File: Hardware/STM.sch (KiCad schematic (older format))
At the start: 17 parts, among them U1 STM32F042K6Ux

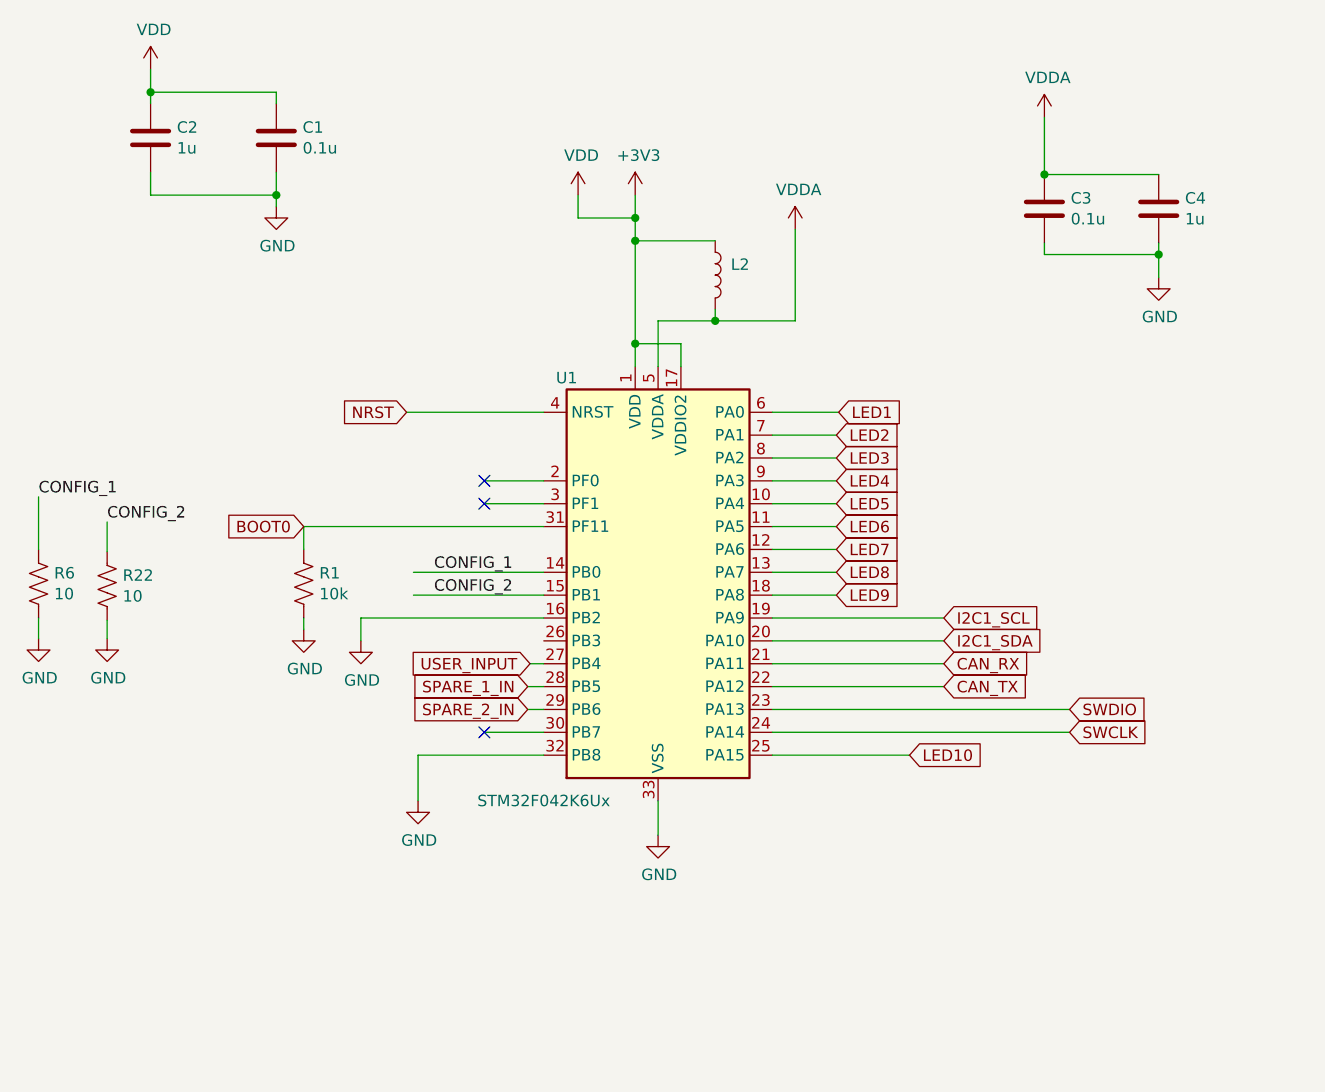
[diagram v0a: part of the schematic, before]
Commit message: Rev B
Update STM package, switcher circuit, layout
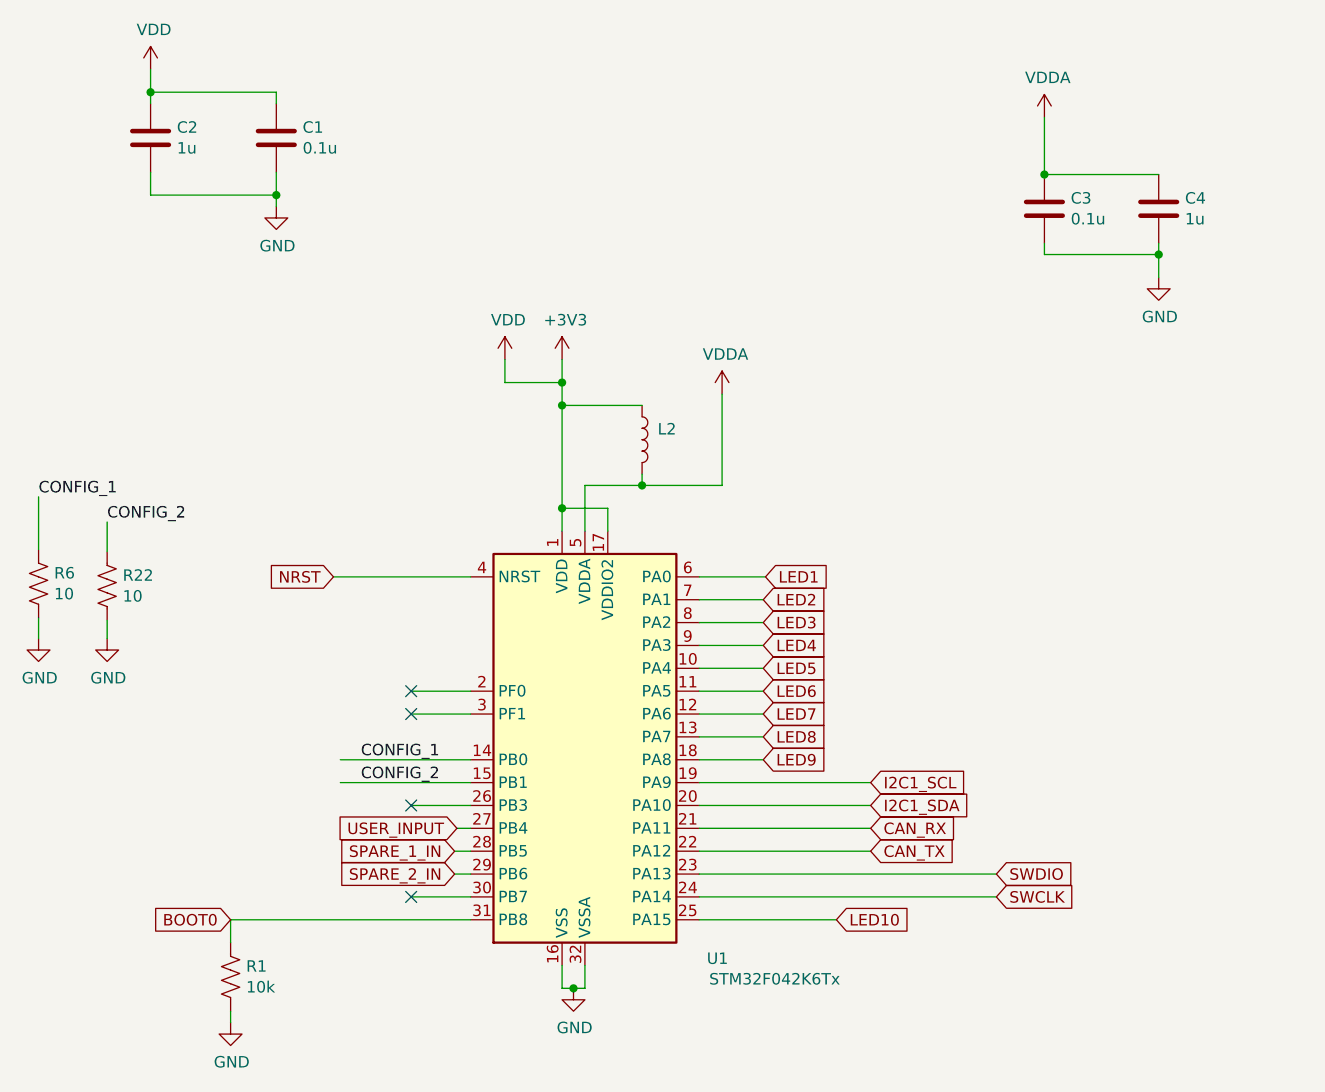
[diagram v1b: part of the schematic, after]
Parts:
- removed U1: STM32F042K6Ux, Package_DFN_QFN:QFN-32-1EP_5x5mm_P0.5mm_EP3.45x3.45mm, symbol MCU_ST_STM32F0:STM32F042K6Ux
- added U1: STM32F042K6Tx, Package_QFP:LQFP-32_7x7mm_P0.8mm, symbol MCU_ST_STM32F0:STM32F042K6Tx
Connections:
- net +3V3: now also U1.1 (VDD), U1.17 (VDDIO2)
- net BOOT0: now also U1.31 (PB8)
- net CAN_RX: now also U1.21 (PA11)
- net CAN_TX: now also U1.22 (PA12)
- net CONFIG_1: now also U1.14 (PB0)
- net CONFIG_2: now also U1.15 (PB1)
- net GND: now also U1.16 (VSS), U1.32 (VSSA)
- net I2C1_SCL: now also U1.19 (PA9)
- net I2C1_SDA: now also U1.20 (PA10)
- net LED1: now also U1.6 (PA0)
- net LED10: now also U1.25 (PA15)
- net LED2: now also U1.7 (PA1)
- net LED3: now also U1.8 (PA2)
- net LED4: now also U1.9 (PA3)
- net LED5: now also U1.10 (PA4)
- net LED6: now also U1.11 (PA5)
- net LED7: now also U1.12 (PA6)
- net LED8: now also U1.13 (PA7)
- net LED9: now also U1.18 (PA8)
- net NRST: now also U1.4 (NRST)
- net SPARE_1_IN: now also U1.28 (PB5)
- net SPARE_2_IN: now also U1.29 (PB6)
- net SWCLK: now also U1.24 (PA14)
- net SWDIO: now also U1.23 (PA13)
- net USER_INPUT: now also U1.27 (PB4)
- net VDDA: now also U1.5 (VDDA)
- no-connect marks 3 -> 4
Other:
- moved on the sheet: L2, R1

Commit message: Update components for assembly, generate gerbers
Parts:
- C1, C3: Comments (none) -> 0402 Multilayer Ceramic Capacitors MLCC - SMD/SMT ROHS; LCSC (none) -> C2655418
- C2: Comment (none) -> X5R ±10% 10V 1uF 0402 Multilayer Ceramic Capacitors MLCC - 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; LCSC (none) -> C389008
- C4: Comments (none) -> X5R ±10% 10V 1uF 0402 Multilayer Ceramic Capacitors MLCC - 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; LCSC (none) -> C389008
- L2: Comments (none) -> 600Ω @ 100MHz 1 500mA 340mΩ 0402 Ferrite Beads ROHS; LCSC (none) -> C76886; Part Number BLM15PE300SH1D -> (none)
- R22, R6: value 10 -> 10k
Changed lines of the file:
@@
 F 2 "Capacitor_SMD:C_0402_1005Metric" H 5978 3020 50  0001 C CNN
 F 3 "~" H 5940 3170 50  0001 C CNN
+F 4 "C389008" H 5940 3170 50  0001 C CNN "LCSC"
+F 5 "X5R ±10% 10V 1uF 0402 Multilayer Ceramic Capacitors MLCC - SMD/SMT ROHS" H 5940 3170 50  0001 C CNN "Comments"
 	1    5940 3170
 	1    0    0    -1
@@
 F 2 "Capacitor_SMD:C_0402_1005Metric" H 5478 3020 50  0001 C CNN
 F 3 "~" H 5440 3170 50  0001 C CNN
+F 4 "C2655418" H 5440 3170 50  0001 C CNN "LCSC"
+F 5 "0402 Multilayer Ceramic Capacitors MLCC - SMD/SMT ROHS" H 5440 3170 50  0001 C CNN "Comments"
 	1    5440 3170
 	1    0    0    -1
@@
 F 2 "Capacitor_SMD:C_0402_1005Metric" H 1568 2710 50  0001 C CNN
 F 3 "~" H 1530 2860 50  0001 C CNN
+F 4 "C389008" H 1530 2860 50  0001 C CNN "LCSC"
+F 5 "X5R ±10% 10V 1uF 0402 Multilayer Ceramic Capacitors MLCC - SMD/SMT ROHS" H 1530 2860 50  0001 C CNN "Comment"
 	1    1530 2860
 	1    0    0    -1
@@
 F 2 "Capacitor_SMD:C_0402_1005Metric" H 2118 2710 50  0001 C CNN
 F 3 "~" H 2080 2860 50  0001 C CNN
+F 4 "C2655418" H 2080 2860 50  0001 C CNN "LCSC"
+F 5 "0402 Multilayer Ceramic Capacitors MLCC - SMD/SMT ROHS" H 2080 2860 50  0001 C CNN "Comments"
 	1    2080 2860
 	1    0    0    -1
@@
 F 2 "Inductor_SMD:L_0402_1005Metric" V 3720 4170 50  0001 C CNN
 F 3 "https://www.murata.com/products/productdata/8796743696414/QNFA9103.pdf" H 3680 4180 50  0001 C CNN
-F 4 "BLM15PE300SH1D" H 3680 4180 50  0001 C CNN "Part Number"
+F 4 "" H 3680 4180 50  0001 C CNN "Part Number"
 F 5 "Murata Electronics" H 3680 4180 50  0001 C CNN "Manufacturer"
+F 6 "C76886" H 3680 4180 50  0001 C CNN "LCSC"
+F 7 "600Ω @ 100MHz 1 500mA 340mΩ 0402 Ferrite Beads ROHS" H 3680 4180 50  0001 C CNN "Comments"
 	1    3680 4180
 	1    0    0    -1
@@
 P 1040 4810
 F 0 "R6" H 1108 4856 50  0000 L CNN
-F 1 "10" H 1108 4765 50  0000 L CNN
+F 1 "10k" H 1108 4765 50  0000 L CNN
 F 2 "Resistor_SMD:R_0402_1005Metric" V 1080 4800 50  0001 C CNN
 F 3 "~" H 1040 4810 50  0001 C CNN
@@
 P 1340 4820
 F 0 "R22" H 1408 4866 50  0000 L CNN
-F 1 "10" H 1408 4775 50  0000 L CNN
+F 1 "10k" H 1408 4775 50  0000 L CNN
 F 2 "Resistor_SMD:R_0402_1005Metric" V 1380 4810 50  0001 C CNN
 F 3 "~" H 1340 4820 50  0001 C CNN

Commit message: Update board layout
Fix OLED pads to meet intended design. Move all non UI components to one side of the board for better single sided assembly.
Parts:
- removed R22, R6: 10k, Resistor_SMD:R_0402_1005Metric, symbol Device:R_US
- added JP2, JP3: SolderJumper_2_Open, Jumper:SolderJumper-2_P1.3mm_Open_Pad1.0x1.5mm, symbol Jumper:SolderJumper_2_Open
- added TP1, TP2: TestPoint, TestPoint:TestPoint_Pad_D1.0mm, symbol Connector:TestPoint
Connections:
- net CONFIG_1: now also JP2.1 (A)
- net CONFIG_2: now also JP3.1 (A)
- net GND: now also JP2.2 (B), JP3.2 (B)
- net I2C1_SCL: now also TP1.1
- net I2C1_SDA: now also TP2.1
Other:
- moved on the sheet: C1, C2
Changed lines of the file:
@@
 $EndComp
 Wire Wire Line
-	9090 3650 8160 3650
+	9090 3650 8180 3650
 Wire Wire Line
 	9090 3450 9090 3650
-Wire Wire Line
-	8750 3500 8160 3500
 Wire Wire Line
 	8750 3450 8750 3500
@@
 	3430 4380 3680 4380
 Wire Wire Line
-	1530 2660 2080 2660
-Wire Wire Line
-	1530 2560 1530 2660
-Connection ~ 1530 2660
-Wire Wire Line
-	1530 2710 1530 2660
+	970  2230 1520 2230
+Wire Wire Line
+	970  2130 970  2230
+Connection ~ 970  2230
+Wire Wire Line
+	970  2280 970  2230
 Wire Wire Line
 	5440 2770 5440 3020
@@
 L power:VDD #PWR0111
 U 1 1 612E9EF6
-P 1530 2560
-F 0 "#PWR0111" H 1530 2410 50  0001 C CNN
-F 1 "VDD" H 1545 2733 50  0000 C CNN
-F 2 "" H 1530 2560 50  0001 C CNN
-F 3 "" H 1530 2560 50  0001 C CNN
-	1    1530 2560
+P 970 2130
+F 0 "#PWR0111" H 970 1980 50  0001 C CNN
+F 1 "VDD" H 985 2303 50  0000 C CNN
+F 2 "" H 970 2130 50  0001 C CNN
+F 3 "" H 970 2130 50  0001 C CNN
+	1    970  2130
 	1    0    0    -1
 $EndComp
@@
 $EndComp
 Wire Wire Line
-	1530 3110 2080 3110
-Wire Wire Line
-	2080 3160 2080 3110
-Connection ~ 2080 3110
-Wire Wire Line
-	2080 3010 2080 3110
-Wire Wire Line
-	1530 3010 1530 3110
+	970  2680 1520 2680
+Wire Wire Line
+	1520 2730 1520 2680
+Connection ~ 1520 2680
+Wire Wire Line
+	1520 2580 1520 2680
+Wire Wire Line
+	970  2580 970  2680
 $Comp
 L Device:C C2
 U 1 1 612D4B72
-P 1530 2860
-F 0 "C2" H 1645 2906 50  0000 L CNN
-F 1 "1u" H 1645 2815 50  0000 L CNN
-F 2 "Capacitor_SMD:C_0402_1005Metric" H 1568 2710 50  0001 C CNN
-F 3 "~" H 1530 2860 50  0001 C CNN
-F 4 "C389008" H 1530 2860 50  0001 C CNN "LCSC"
-F 5 "X5R ±10% 10V 1uF 0402 Multilayer Ceramic Capacitors MLCC - SMD/SMT ROHS" H 1530 2860 50  0001 C CNN "Comment"
-	1    1530 2860
-	1    0    0    -1
-$EndComp
-Wire Wire Line
-	2080 2710 2080 2660
+P 970 2430
+F 0 "C2" H 1085 2476 50  0000 L CNN
+F 1 "1u" H 1085 2385 50  0000 L CNN
+F 2 "Capacitor_SMD:C_0402_1005Metric" H 1008 2280 50  0001 C CNN
+F 3 "~" H 970 2430 50  0001 C CNN
+F 4 "C389008" H 970 2430 50  0001 C CNN "LCSC"
+F 5 "X5R ±10% 10V 1uF 0402 Multilayer Ceramic Capacitors MLCC - SMD/SMT ROHS" H 970 2430 50  0001 C CNN "Comment"
+	1    970  2430
+	1    0    0    -1
+$EndComp
+Wire Wire Line
+	1520 2280 1520 2230
 $Comp
 L power:GND #PWR0114
 U 1 1 612D4205
-P 2080 3160
-F 0 "#PWR0114" H 2080 2910 50  0001 C CNN
-F 1 "GND" H 2085 2987 50  0000 C CNN
-F 2 "" H 2080 3160 50  0001 C CNN
-F 3 "" H 2080 3160 50  0001 C CNN
-	1    2080 3160
+P 1520 2730
+F 0 "#PWR0114" H 1520 2480 50  0001 C CNN
+F 1 "GND" H 1525 2557 50  0000 C CNN
+F 2 "" H 1520 2730 50  0001 C CNN
+F 3 "" H 1520 2730 50  0001 C CNN
+	1    1520 2730
 	1    0    0    -1
 $EndComp
@@
 L Device:C C1
 U 1 1 612CF94B
-P 2080 2860
-F 0 "C1" H 2195 2906 50  0000 L CNN
-F 1 "0.1u" H 2195 2815 50  0000 L CNN
-F 2 "Capacitor_SMD:C_0402_1005Metric" H 2118 2710 50  0001 C CNN
-F 3 "~" H 2080 2860 50  0001 C CNN
-F 4 "C2655418" H 2080 2860 50  0001 C CNN "LCSC"
-F 5 "0402 Multilayer Ceramic Capacitors MLCC - SMD/SMT ROHS" H 2080 2860 50  0001 C CNN "Comments"
-	1    2080 2860
+P 1520 2430
+F 0 "C1" H 1635 2476 50  0000 L CNN
+F 1 "0.1u" H 1635 2385 50  0000 L CNN
+F 2 "Capacitor_SMD:C_0402_1005Metric" H 1558 2280 50  0001 C CNN
+F 3 "~" H 1520 2430 50  0001 C CNN
+F 4 "C2655418" H 1520 2430 50  0001 C CNN "LCSC"
+F 5 "0402 Multilayer Ceramic Capacitors MLCC - SMD/SMT ROHS" H 1520 2430 50  0001 C CNN "Comments"
+	1    1520 2430
 	1    0    0    -1
 $EndComp
@@
 Text Label 2450 5680 0    50   ~ 0
 CONFIG_2
-$Comp
-L Device:R_US R6
-U 1 1 616B061C
-P 1040 4810
-F 0 "R6" H 1108 4856 50  0000 L CNN
-F 1 "10k" H 1108 4765 50  0000 L CNN
-F 2 "Resistor_SMD:R_0402_1005Metric" V 1080 4800 50  0001 C CNN
-F 3 "~" H 1040 4810 50  0001 C CNN
-	1    1040 4810
-	1    0    0    -1
-$EndComp
-$Comp
-L Device:R_US R22
-U 1 1 616B28A7
-P 1340 4820
-F 0 "R22" H 1408 4866 50  0000 L CNN
-F 1 "10k" H 1408 4775 50  0000 L CNN
-F 2 "Resistor_SMD:R_0402_1005Metric" V 1380 4810 50  0001 C CNN
-F 3 "~" H 1340 4820 50  0001 C CNN
-	1    1340 4820
-	1    0    0    -1
-$EndComp
 Text Label 1040 4430 0    50   ~ 0
 CONFIG_1
-Text Label 1340 4540 0    50   ~ 0
+Text Label 1070 3570 0    50   ~ 0
 CONFIG_2
 Wire Wire Line
-	1340 4540 1340 4670
+	1070 3570 1070 3700
 Wire Wire Line
 	1040 4430 1040 4660
@@
 	1040 4960 1040 5050
 Wire Wire Line
-	1340 4970 1340 5050
+	1070 4000 1070 4080
 $Comp
 L power:GND #PWR0107
 U 1 1 616CEB78
-P 1340 5050
-F 0 "#PWR0107" H 1340 4800 50  0001 C CNN
-F 1 "GND" H 1345 4877 50  0000 C CNN
-F 2 "" H 1340 5050 50  0001 C CNN
-F 3 "" H 1340 5050 50  0001 C CNN
-	1    1340 5050
+P 1070 4080
+F 0 "#PWR0107" H 1070 3830 50  0001 C CNN
+F 1 "GND" H 1075 3907 50  0000 C CNN
+F 2 "" H 1070 4080 50  0001 C CNN
+F 3 "" H 1070 4080 50  0001 C CNN
+	1    1070 4080
 	1    0    0    -1
 $EndComp
@@
 	3430 6580 3430 6480
 Connection ~ 3380 6580
+$Comp
+L Connector:TestPoint TP1
+U 1 1 61B59AAD
+P 8260 3250
+F 0 "TP1" H 8318 3368 50  0000 L CNN
+F 1 "TestPoint" H 8318 3277 50  0000 L CNN
+F 2 "TestPoint:TestPoint_Pad_D1.0mm" H 8460 3250 50  0001 C CNN
+F 3 "~" H 8460 3250 50  0001 C CNN
+	1    8260 3250
+	1    0    0    -1
+$EndComp
+$Comp
+L Connector:TestPoint TP2
+U 1 1 61B5F660
+P 8260 4020
+F 0 "TP2" H 8318 4138 50  0000 L CNN
+F 1 "TestPoint" H 8318 4047 50  0000 L CNN
+F 2 "TestPoint:TestPoint_Pad_D1.0mm" H 8460 4020 50  0001 C CNN
+F 3 "~" H 8460 4020 50  0001 C CNN
+	1    8260 4020
+	1    0    0    -1
+$EndComp
+Wire Wire Line
+	8260 3250 8260 3500
+Wire Wire Line
+	8160 3500 8260 3500
+Connection ~ 8260 3500
+Wire Wire Line
+	8260 3500 8750 3500
+Wire Wire Line
+	8260 4020 8180 4020
+Wire Wire Line
+	8180 4020 8180 3650
+Connection ~ 8180 3650
+Wire Wire Line
+	8180 3650 8160 3650
+$Comp
+L Jumper:SolderJumper_2_Open JP?
+U 1 1 61BBD276
+P 1040 4810
+AR Path="/615E795E/61BBD276" Ref="JP?"  Part="1"
+AR Path="/615E5281/61BBD276" Ref="JP2"  Part="1"
+F 0 "JP2" V 994 4878 50  0000 L CNN
+F 1 "SolderJumper_2_Open" V 1085 4878 50  0000 L CNN
+F 2 "Jumper:SolderJumper-2_P1.3mm_Open_Pad1.0x1.5mm" H 1040 4810 50  0001 C CNN
+F 3 "~" H 1040 4810 50  0001 C CNN
+	1    1040 4810
+	0    1    1    0
+$EndComp
+$Comp
+L Jumper:SolderJumper_2_Open JP?
+U 1 1 61BBFC2A
+P 1070 3850
+AR Path="/615E795E/61BBFC2A" Ref="JP?"  Part="1"
+AR Path="/615E5281/61BBFC2A" Ref="JP3"  Part="1"
+AR Path="/615E8210/61BBFC2A" Ref="JP3"  Part="1"
+F 0 "JP3" V 1024 3918 50  0000 L CNN
+F 1 "SolderJumper_2_Open" V 1115 3918 50  0000 L CNN
+F 2 "Jumper:SolderJumper-2_P1.3mm_Open_Pad1.0x1.5mm" H 1070 3850 50  0001 C CNN
+F 3 "~" H 1070 3850 50  0001 C CNN
+	1    1070 3850
+	0    1    1    0
+$EndComp
 $EndSCHEMATC

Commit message: Updates
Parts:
- R10, R11, R12, R13, R14, R15: Populate DNP -> (none)
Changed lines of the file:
@@
 Title "CAN Gauge"
 Date "2021-10-10"
-Rev "B"
+Rev "C"
 Comp ""
 Comment1 ""
@@
 F 2 "Resistor_SMD:R_0402_1005Metric" V 9340 5030 50  0001 C CNN
 F 3 "~" H 9300 5040 50  0001 C CNN
-F 4 "DNP" H 9160 5170 50  0000 C CNN "Populate"
+F 4 "" H 9160 5170 50  0000 C CNN "Populate"
 	1    9300 5040
 	-1   0    0    1
@@
 F 2 "Resistor_SMD:R_0402_1005Metric" V 8190 5360 50  0001 C CNN
 F 3 "~" H 8150 5370 50  0001 C CNN
-F 4 "DNP" V 7855 5370 50  0000 C CNN "Populate"
+F 4 "" V 7855 5370 50  0000 C CNN "Populate"
 	1    8150 5370
 	0    -1   -1   0
@@
 F 2 "Resistor_SMD:R_0402_1005Metric" V 9500 5650 50  0001 C CNN
 F 3 "~" H 9460 5660 50  0001 C CNN
-F 4 "DNP" H 9320 5790 50  0000 C CNN "Populate"
+F 4 "" H 9320 5790 50  0000 C CNN "Populate"
 	1    9460 5660
 	-1   0    0    1
@@
 F 2 "Resistor_SMD:R_0402_1005Metric" V 9950 5060 50  0001 C CNN
 F 3 "~" H 9910 5070 50  0001 C CNN
-F 4 "DNP" H 9780 5200 50  0000 C CNN "Populate"
+F 4 "" H 9780 5200 50  0000 C CNN "Populate"
 	1    9910 5070
 	-1   0    0    1
@@
 F 2 "Resistor_SMD:R_0402_1005Metric" V 9270 5650 50  0001 C CNN
 F 3 "~" H 9230 5660 50  0001 C CNN
-F 4 "DNP" H 9370 5790 50  0000 C CNN "Populate"
+F 4 "" H 9370 5790 50  0000 C CNN "Populate"
 	1    9230 5660
 	-1   0    0    1
@@
 F 2 "Resistor_SMD:R_0402_1005Metric" V 8460 5260 50  0001 C CNN
 F 3 "~" H 8420 5270 50  0001 C CNN
-F 4 "DNP" V 8533 5270 50  0000 C CNN "Populate"
+F 4 "" V 8533 5270 50  0000 C CNN "Populate"
 	1    8420 5270
 	0    -1   -1   0

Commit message: Update for F103
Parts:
- removed U1: STM32F042K6Tx, Package_QFP:LQFP-32_7x7mm_P0.8mm, symbol MCU_ST_STM32F0:STM32F042K6Tx
- added U1: STM32F103C8Tx, Package_QFP:LQFP-48_7x7mm_P0.5mm, symbol MCU_ST_STM32F1:STM32F103C8Tx
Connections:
- net +3V3: now also U1.24 (VDD), U1.36 (VDD), U1.48 (VDD)
- net BOOT0: now also U1.44 (BOOT0)
- net CAN_RX: now also U1.32 (PA11)
- net CAN_TX: now also U1.33 (PA12)
- net CONFIG_1: now also U1.18 (PB0)
- net CONFIG_2: now also U1.19 (PB1)
- net GND: now also U1.23 (VSS), U1.35 (VSS), U1.47 (VSS), U1.8 (VSSA)
- net I2C1_SCL: now also U1.42 (PB6)
- net I2C1_SDA: now also U1.43 (PB7)
- net LED1: now also U1.10 (PA0)
- net LED10: now also U1.30 (PA9)
- net LED2: now also U1.11 (PA1)
- net LED3: now also U1.12 (PA2)
- net LED4: now also U1.13 (PA3)
- net LED5: now also U1.14 (PA4)
- net LED6: now also U1.15 (PA5)
- net LED7: now also U1.16 (PA6)
- net LED8: now also U1.17 (PA7)
- net LED9: now also U1.29 (PA8)
- net NRST: now also U1.7 (NRST)
- net SPARE_1_IN: now also U1.39 (PB3)
- net SPARE_2_IN: now also U1.40 (PB4)
- net SWCLK: now also U1.37 (PA14)
- net SWDIO: now also U1.34 (PA13)
- net USER_INPUT: now also U1.38 (PA15)
- net VDDA: now also U1.9 (VDDA)
- new net OSC_IN: U1.3 (PC14)
- new net OSC_OUT: U1.4 (PC15)
- no-connect marks 4 -> 0
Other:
- moved on the sheet: C3, C4, JP2, JP3, L2, R1, R10, R11, R12, R13, R14, R15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

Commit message: Work in progress
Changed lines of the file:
@@
 Text GLabel 2200 4690 0    50   Input ~ 0
-OSC_OUT
-Text GLabel 5020 3830 0    50   Input ~ 0
-OSC_IN
-Text GLabel 5030 4120 0    50   Input ~ 0
 OSC_OUT
 Wire Wire Line

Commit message: Update pcb
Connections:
- net labels added: CONFIG_3, CONFIG_4, CONFIG_5
- wire segments 94 -> 98
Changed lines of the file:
@@
 Wire Wire Line
 	4160 6390 3970 6390
+Wire Wire Line
+	2660 5090 1580 5090
+Wire Wire Line
+	1580 5090 1580 5100
+Wire Wire Line
+	2670 5890 1680 5890
+Wire Wire Line
+	2670 5990 1680 5990
+Text Label 1700 5090 0    50   ~ 0
+CONFIG_3
+Text Label 1820 5890 0    50   ~ 0
+CONFIG_4
+Text Label 1820 5990 0    50   ~ 0
+CONFIG_5
 $EndSCHEMATC

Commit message: Generate files
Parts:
- U1: LCSC (none) -> C8734; Package (none) -> LQFP48
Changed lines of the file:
@@
 F 2 "Package_QFP:LQFP-48_7x7mm_P0.5mm" H 2770 3690 50  0001 R CNN
 F 3 "http://www.st.com/st-web-ui/static/active/en/resource/technical/document/datasheet/CD00161566.pdf" H 3370 5090 50  0001 C CNN
+F 4 "C8734 " H 3370 5090 50  0001 C CNN "LCSC"
+F 5 "LQFP48 " H 3370 5090 50  0001 C CNN "Package"
 	1    3370 5090
 	1    0    0    -1
